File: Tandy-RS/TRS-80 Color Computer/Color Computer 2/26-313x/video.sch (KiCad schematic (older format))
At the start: 5 parts, among them SW3 SW_SPDT

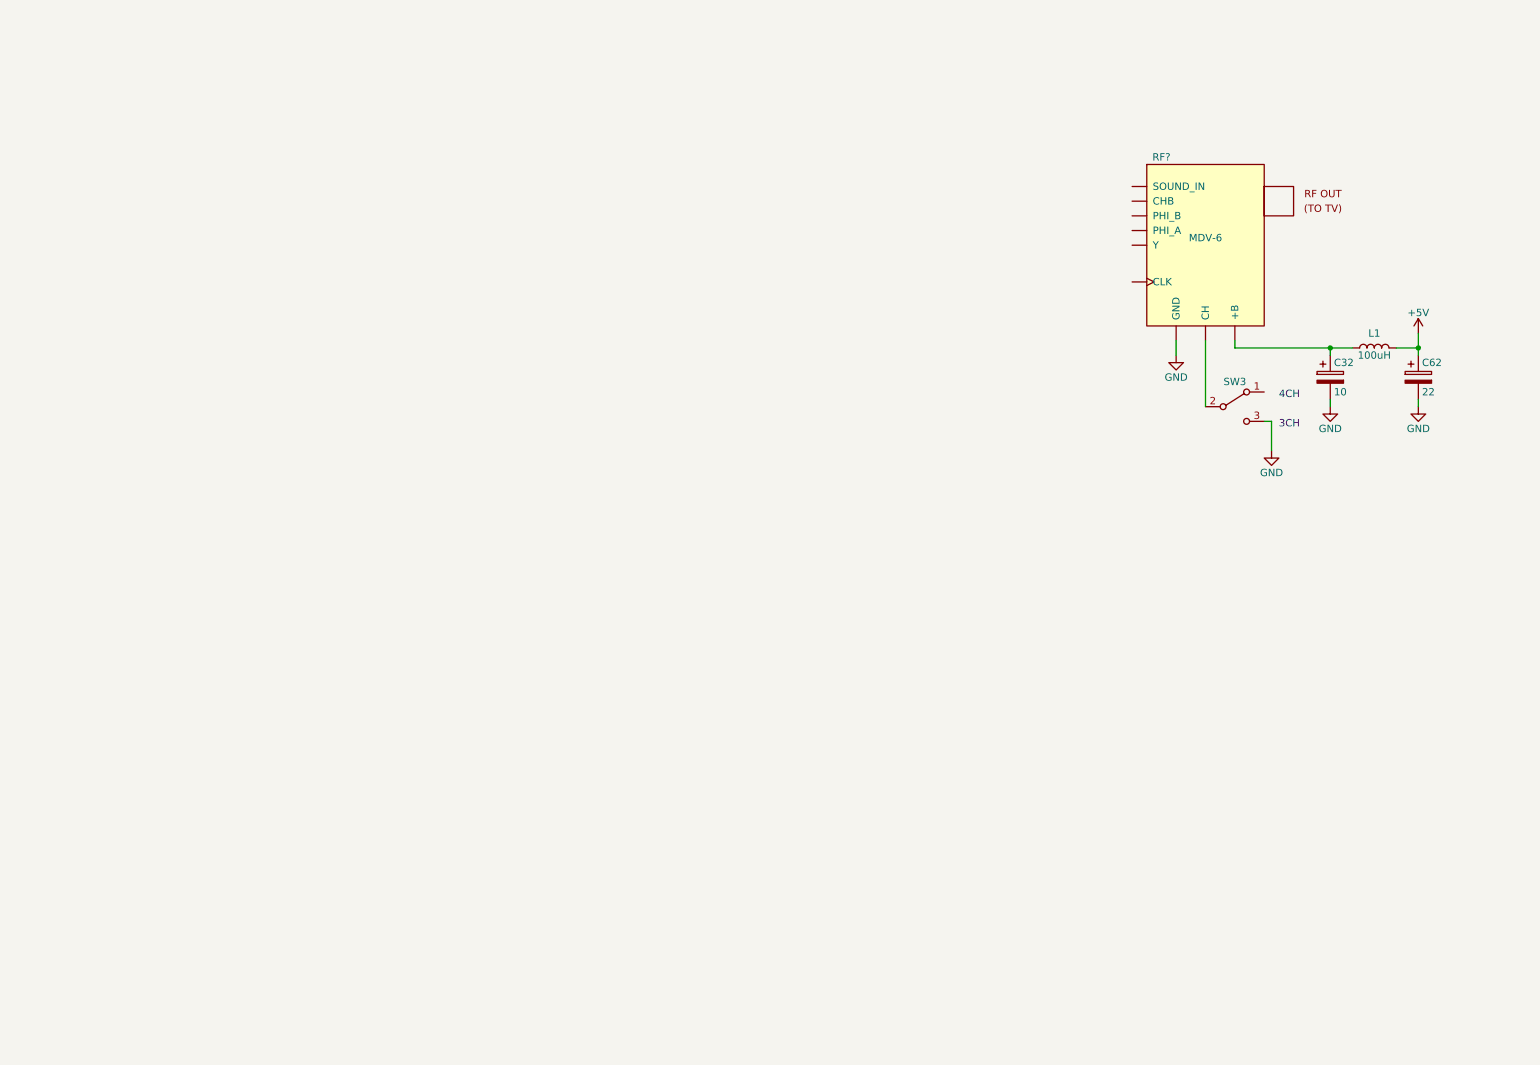
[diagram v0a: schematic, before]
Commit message: Complete video schematic
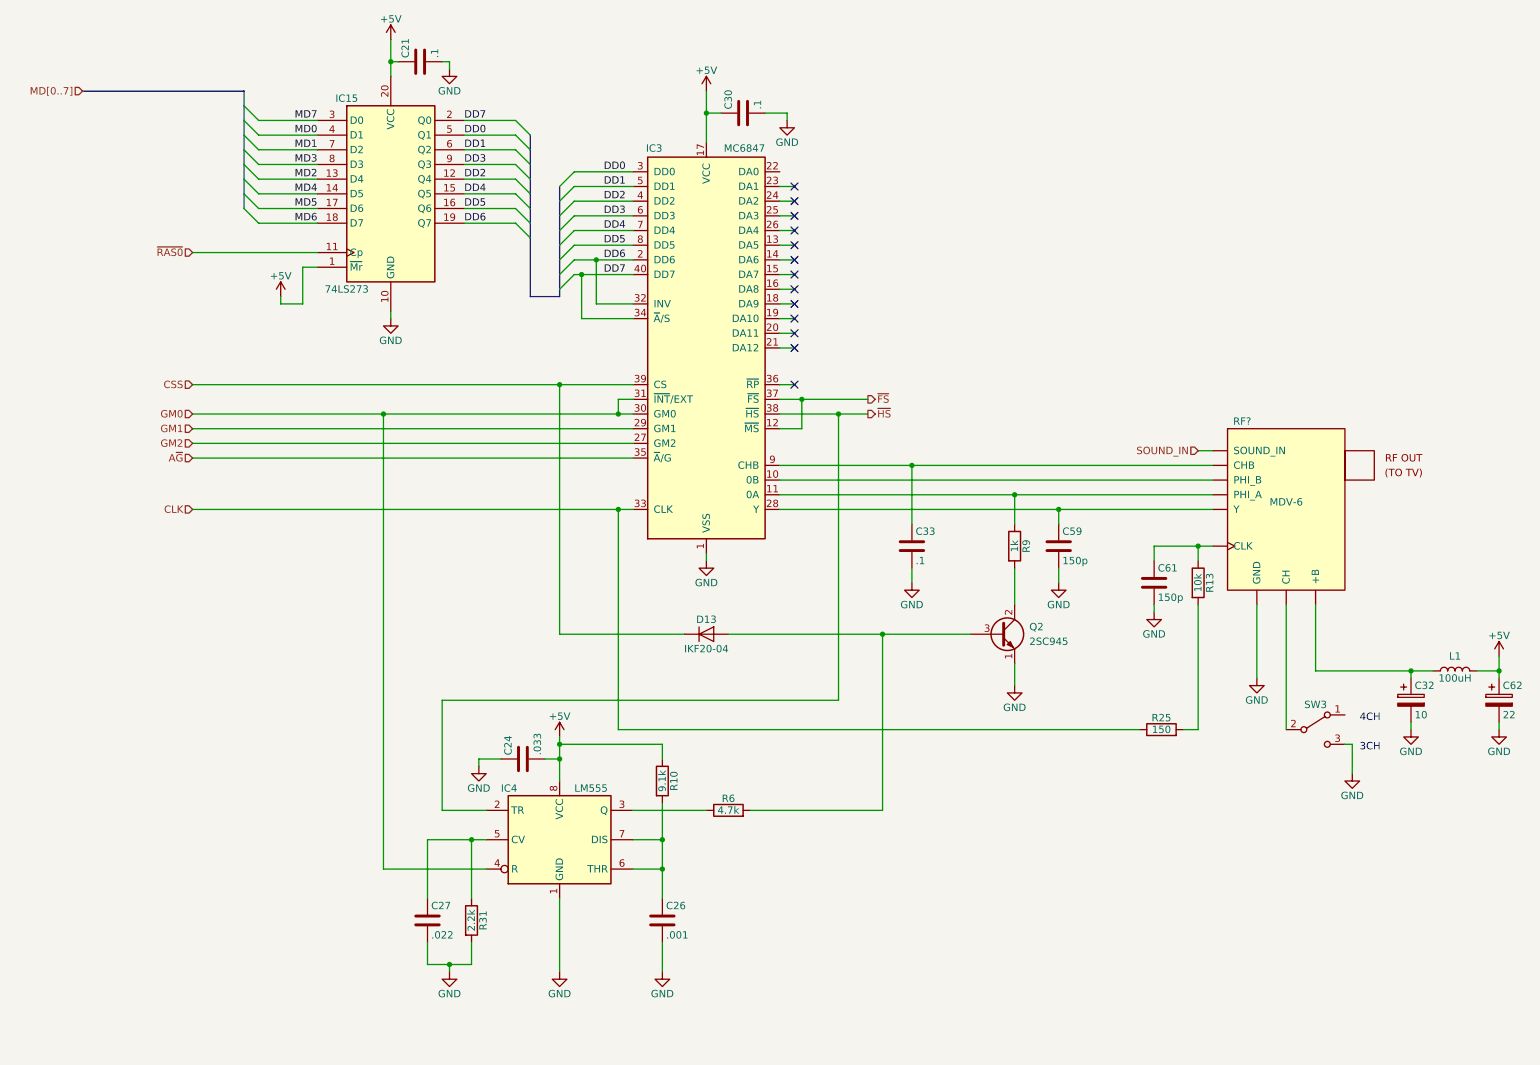
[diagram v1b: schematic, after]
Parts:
- added C21, C30, C33: .1, symbol Device:C
- added C24: .033, symbol Device:C
- added C26: .001, symbol Device:C
- added C27: .022, symbol Device:C
- added C59, C61: 150p, symbol Device:C
- added D13: IKF20-04, symbol Device:D
- added IC15: 74LS273, symbol 74xx:74LS273
- added IC3: MC6847, Package_DIP:DIP-40_W15.24mm, symbol Video_Motorola:MC6847
- added IC4: LM555, symbol Timer:LM555
- added Q2: 2SC945, symbol Device:Q_NPN_ECB
- added R10: 9.1k, symbol Device:R
- added R13: 10k, symbol Device:R
- added R25: 150, symbol Device:R
- added R31: 2.2k, symbol Device:R
- added R6: 4.7k, symbol Device:R
- added R9: 1k, symbol Device:R
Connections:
- net +5V: now also C21.1, C24.2, C30.1, IC15.1 (~Mr), IC15.20 (VCC), IC3.17 (VCC), IC4.8 (VCC), R10.1
- net GND: now also C21.2, C24.1, C26.2, C27.2, C30.2, C33.2, C59.2, C61.2, IC15.10 (GND), IC3.1 (VSS), IC4.1 (GND), Q2.1 (E), R31.2
- net at RF?.2 (PHI_A): now also IC3.11 (0A), R9.1
- net SOUND_IN: now reaches RF?.~ (Y)
- new net: IC3.10 (0B), RF?.~ (Y)
- new net: C59.1, IC3.28 (Y), RF?.~ (Y)
- new net: C33.1, IC3.9 (CHB), RF?.~ (Y)
- new net: C61.1, R13.1, RF?.~ (Y)
- new net: IC4.3 (Q), R6.1
- new net: C27.1, IC4.5 (CV), R31.1
- new net: C26.1, IC4.6 (THR), IC4.7 (DIS), R10.2
- new net: D13.2 (A), Q2.3 (B), R6.2
- new net: Q2.2 (C), R9.2
- new net: R13.2, R25.2
- new net A~G: IC3.35 (~A~/G)
- new net CLK: IC3.33 (CLK), R25.1
- new net CSS: D13.1 (K), IC3.39 (CS)
- new net DD0: IC15.5 (Q1), IC3.3 (DD0)
- new net DD1: IC15.6 (Q2), IC3.5 (DD1)
- new net DD2: IC15.12 (Q4), IC3.4 (DD2)
- new net DD3: IC15.9 (Q3), IC3.6 (DD3)
- new net DD4: IC15.15 (Q5), IC3.7 (DD4)
- new net DD5: IC15.16 (Q6), IC3.8 (DD5)
- new net DD6: IC15.19 (Q7), IC3.2 (DD6), IC3.32 (INV)
- new net DD7: IC15.2 (Q0), IC3.34 (~A~/S), IC3.40 (DD7)
- new net GM0: IC3.30 (GM0), IC3.31 (~INT~/EXT), IC4.4 (R)
- new net GM1: IC3.29 (GM1)
- new net GM2: IC3.27 (GM2)
- new net MD0: IC15.4 (D1)
- new net MD1: IC15.7 (D2)
- new net MD2: IC15.13 (D4)
- new net MD3: IC15.8 (D3)
- new net MD4: IC15.14 (D5)
- new net MD5: IC15.17 (D6)
- new net MD6: IC15.18 (D7)
- new net MD7: IC15.3 (D0)
- new net ~FS: IC3.12 (~MS), IC3.37 (~FS)
- new net ~HS: IC3.38 (~HS), IC4.2 (TR)
- new net ~RAS0: IC15.11 (Cp)
- no-connect marks 0 -> 13
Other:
- moved on the sheet: C32, C62, L1, RF?, SW3

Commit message: Finish drawing initial version of Coco2 schematic
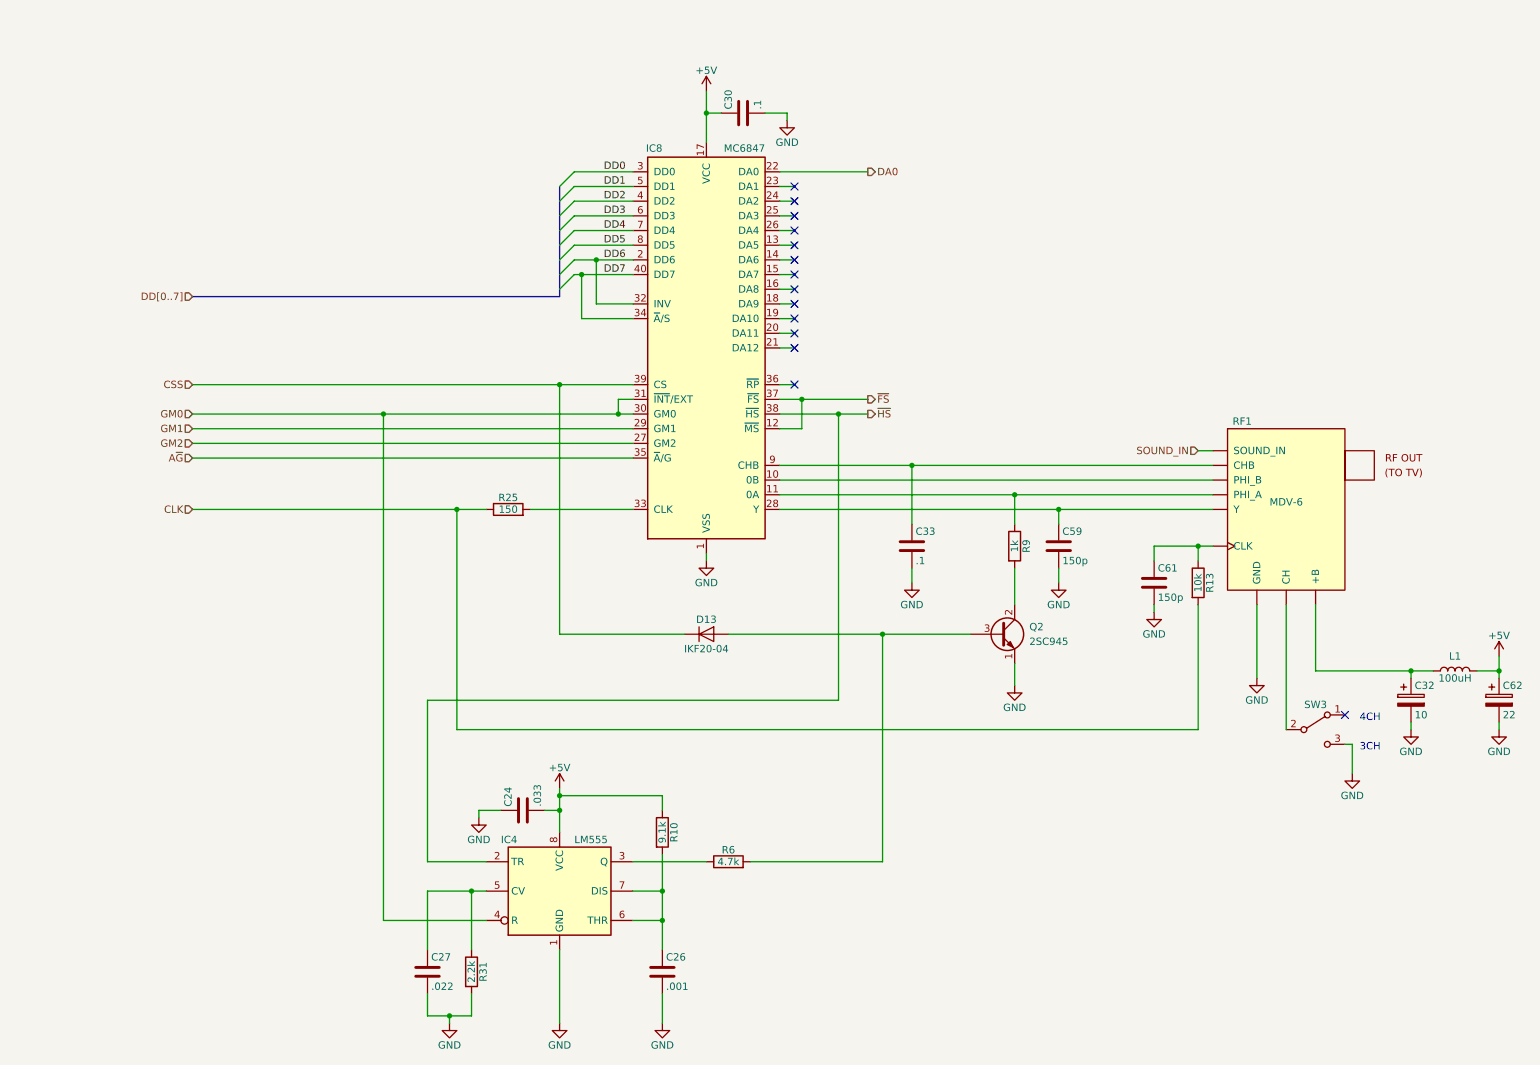
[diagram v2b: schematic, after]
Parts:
- removed C21: .1, symbol Device:C
- removed IC15: 74LS273, symbol 74xx:74LS273
- gave numbers to parts that had none: 1
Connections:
- net CLK: now also R13.2; no longer IC3.33 (CLK)
- net DA0: now reaches IC3.22 (DA0)
- net at R25.2: now also IC3.33 (CLK); no longer R13.2
- no-connect marks 13 -> 14
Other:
- moved on the sheet: C24, C26, C27, IC4, R10, R25, R31, R6
